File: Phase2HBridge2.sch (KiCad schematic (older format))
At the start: 42 parts, among them J1 CONN-01X06-TerminalBlock-3.5m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, J2 CONN-FASTON-0.250\"-1217861-1, J3 CONN-FASTON-0.250\"-1217861-1, J4 CONN-FASTON-0.250\"-1217861-1, J5 CONN-FASTON-0.250\"-1217861-1, Q1 FET-NCH-400V-26A-TO220-FDP26N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, Q2 FET-NCH-400V-26A-TO220-FDP26N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, Q3 FET-NCH-400V-26A-TO220-FDP26N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, Q4 FET-NCH-400V-26A-TO220-FDP26N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, U1 IC-Driver-HalfBridge-FAN7393A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

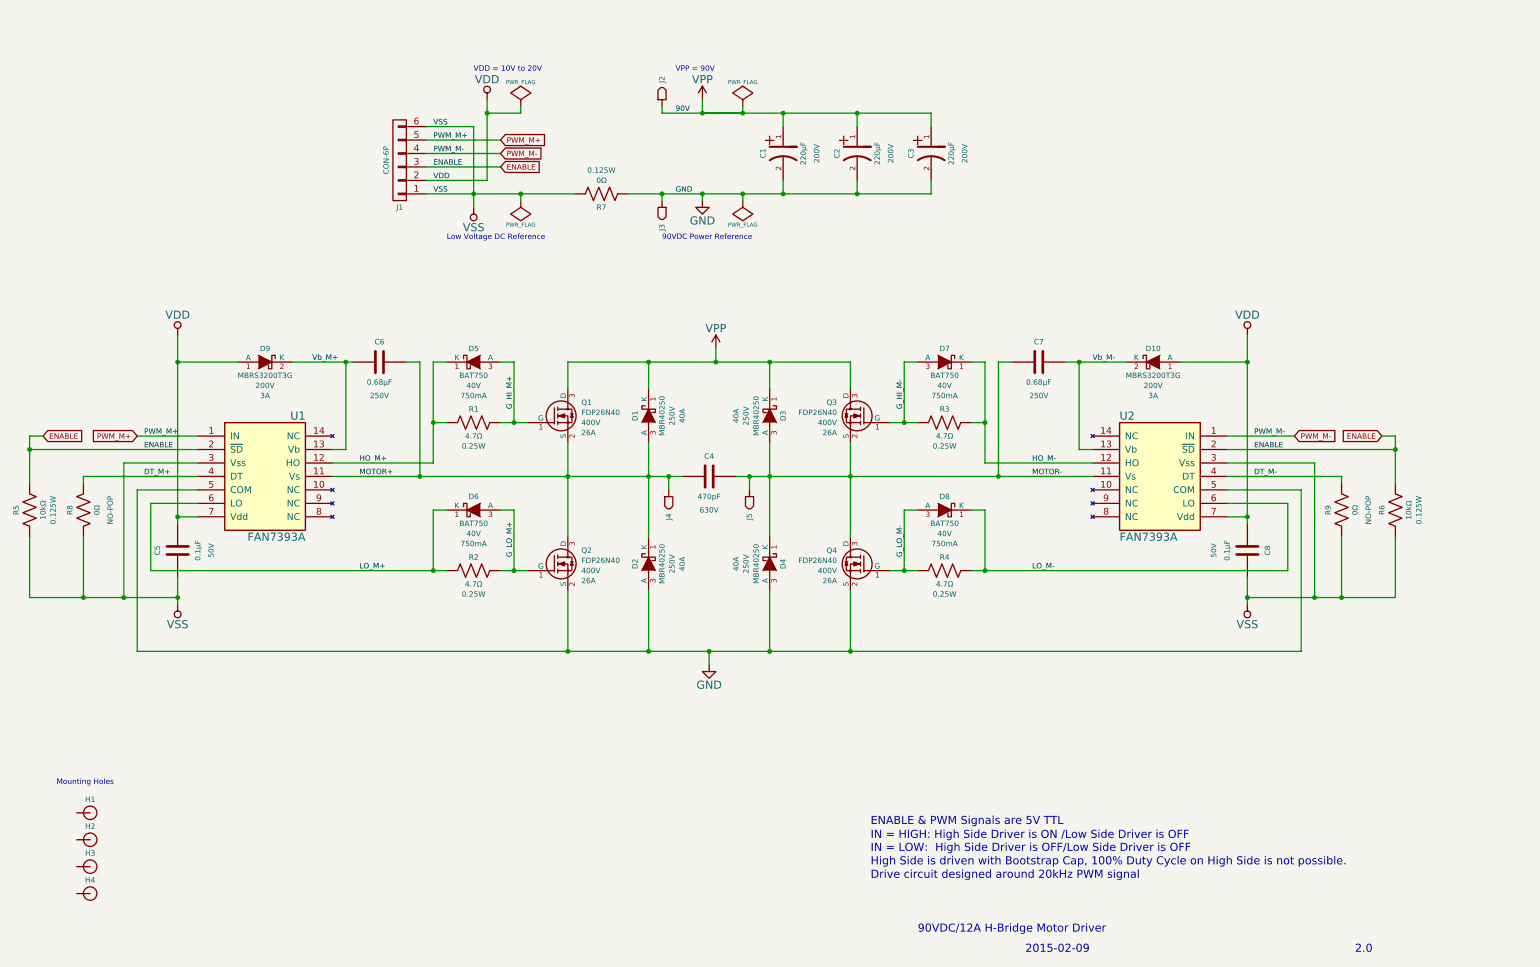
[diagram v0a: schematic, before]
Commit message: Finished Layout
Need to Verify Layout, add graphics, update refused locations, etc…
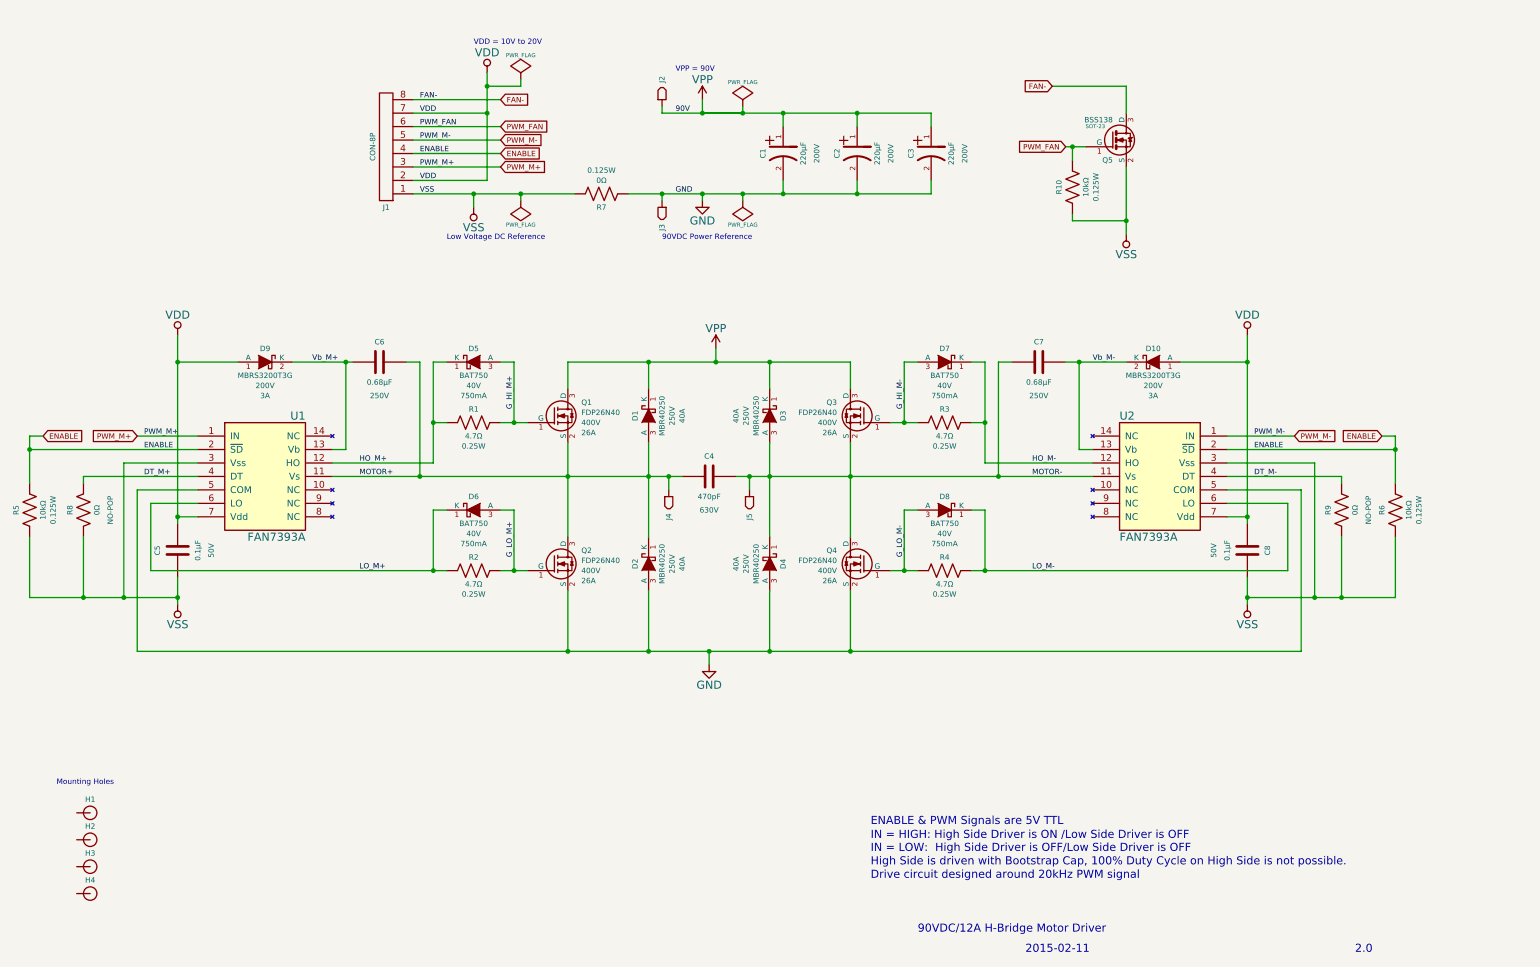
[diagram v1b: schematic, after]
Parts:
- removed J1: CONN-01X06-TerminalBlock-3.5mm-Side-1776275-6, Phase2HBridge2:CON-TerminalBlock-6Pos-Side-3.5MM-1776275-6, symbol CONN-01X06-TerminalBlock-3.5mm-Side-1776275-6
- added J1: CONN-01X08-TerminalBlock-3.5mm-Side-1776275-8, Phase2HBridge2:CON-TerminalBlock-8Pos-Side-3.5MM-1776275-8, symbol CONN-01X08-TerminalBlock-3.5mm-Side-1776275-8
- added Q5: BSS138, SOT-23, symbol BSS138
- added R10: RES-10k-.125W-1%-0805-ERJ-6ENF1002V, Resistors_SMD:R_0805, symbol RES-10k-.125W-1%-0805-ERJ-6ENF1002V
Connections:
- net ENABLE: now also J1.4 (P4)
- net PWM_M+: now also J1.3 (P3)
- net PWM_M-: now also J1.5 (P5)
- net VDD: now also J1.2 (P2), J1.7 (P7)
- net VSS: now also J1.1 (P1), Q5.2 (S), R10.2
- new net FAN-: J1.8 (P8), Q5.3 (D)
- new net PWM_FAN: J1.6 (P6), Q5.1 (G), R10.1
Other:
- note added: "2015-02-11"
- note removed: "2015-02-09"
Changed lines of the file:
@@
-$EndComp
-$Comp
-L CONN-01X06-TerminalBlock-3.5mm-Side-1776275-6 J1
-U 1 1 54D9000B
-P 3500 1750
-F 0 "J1" H 3500 2100 40  0000 C CNN
-F 1 "CONN-01X06-TerminalBlock-3.5mm-Side-1776275-6" H 3500 2300 40  0001 L CNN
-F 2 "Phase2HBridge2:CON-TerminalBlock-6Pos-Side-3.5MM-1776275-6" H 3500 1050 40  0001 L CNN
-F 3 "http://www.te.com/commerce/DocumentDelivery/DDEController?Action=srchrtrv&DocNm=1776275&DocType=Customer+Drawing&DocLang=English" H 3500 825 40  0001 L CNN
-F 4 "TE Connectivity" H 3500 950 40  0001 L CNN "MFG"
-F 5 "1776275-6" H 3500 900 40  0001 L CNN "MFGPN"
-F 6 "DigiKey" H 3500 700 40  0001 L CNN "CR1"
-F 7 "A98040-ND" H 3500 650 40  0001 L CNN "CR1PN"
-F 8 "-55°C:105°C" H 3500 525 40  0001 L CNN "Temp"
-F 9 "2015-02-09" H 3500 375 40  0001 L CNN "Created"
-F 10 "XXXX-XX-XX" H 3500 300 40  0001 L CNN "Verified"
-F 11 "CON-6P" V 3600 1750 40  0000 C CNN "Value.Display"
-	1    3500 1750
-	-1   0    0    1
 $EndComp
 $Comp
@@
 Connection ~ 5450 2000
 Wire Wire Line
-	3700 2000 4800 2000
+	3600 2000 4800 2000
 Wire Wire Line
 	5800 5400 5800 5500
@@
 	10200 4200 10200 5400
 Connection ~ 6850 5400
-Text Notes 4050 1100 0    40   ~ 0
+Text Notes 4050 900  0    40   ~ 0
 VDD = 10V to 20V
 Text Notes 5550 1100 0    40   ~ 0
@@
 Text Notes 950  6400 0    40   ~ 0
 Mounting Holes
-Text Label 3750 2000 0    40   ~ 0
+Text Label 3650 2000 0    40   ~ 0
 VSS
-Text Label 3750 1900 0    40   ~ 0
+Text Label 3650 1900 0    40   ~ 0
 VDD
 Text Label 5550 2000 0    40   ~ 0
@@
 Text Label 5550 1400 0    40   ~ 0
 90V
-Text Label 3750 1500 0    40   ~ 0
-VSS
+Text GLabel 4250 1800 2    40   Input ~ 0
+PWM_M+
 Text GLabel 4250 1600 2    40   Input ~ 0
+PWM_M-
+Text GLabel 4250 1700 2    40   Input ~ 0
+ENABLE
+Text Label 3650 1800 0    40   ~ 0
 PWM_M+
-Text GLabel 4250 1700 2    40   Input ~ 0
+Text Label 3650 1600 0    40   ~ 0
 PWM_M-
-Text GLabel 4250 1800 2    40   Input ~ 0
-ENABLE
-Wire Wire Line
-	3700 1600 4250 1600
-Wire Wire Line
-	3700 1700 4250 1700
-Wire Wire Line
-	3700 1800 4250 1800
-Text Label 3750 1600 0    40   ~ 0
-PWM_M+
-Text Label 3750 1700 0    40   ~ 0
-PWM_M-
-Text Label 3750 1800 0    40   ~ 0
+Text Label 3650 1700 0    40   ~ 0
 ENABLE
 Text GLabel 1550 3800 0    40   Input ~ 0
@@
 Text Label 1600 3800 0    40   ~ 0
 PWM_M+
-Wire Wire Line
-	4050 1500 4050 2100
 Connection ~ 4050 2000
-Wire Wire Line
-	3700 1500 4050 1500
 $Comp
 L VSS #PWR01
@@
 L VDD #PWR06
 U 1 1 54DAE29D
-P 4150 1300
-F 0 "#PWR06" H 4150 1150 60  0001 C CNN
-F 1 "VDD" H 4150 1450 60  0000 C CNN
-F 2 "" H 4150 1300 60  0000 C CNN
-F 3 "" H 4150 1300 60  0000 C CNN
-	1    4150 1300
+P 4150 1100
+F 0 "#PWR06" H 4150 950 60  0001 C CNN
+F 1 "VDD" H 4150 1250 60  0000 C CNN
+F 2 "" H 4150 1100 60  0000 C CNN
+F 3 "" H 4150 1100 60  0000 C CNN
+	1    4150 1100
 	1    0    0    -1
 $EndComp
@@
 $EndComp
 Wire Wire Line
-	4150 1300 4150 1900
-Wire Wire Line
-	4150 1900 3700 1900
+	4150 1100 4150 1900
+Wire Wire Line
+	4150 1900 3600 1900
 $Comp
 L VPP #PWR010
@@
 L PWR_FLAG #FLG013
 U 1 1 54DB25F7
-P 4400 1350
-F 0 "#FLG013" H 4400 1445 30  0001 C CNN
-F 1 "PWR_FLAG" H 4400 1530 30  0000 C CNN
-F 2 "" H 4400 1350 60  0000 C CNN
-F 3 "" H 4400 1350 60  0000 C CNN
-	1    4400 1350
+P 4400 1150
+F 0 "#FLG013" H 4400 1245 30  0001 C CNN
+F 1 "PWR_FLAG" H 4400 1330 30  0000 C CNN
+F 2 "" H 4400 1150 60  0000 C CNN
+F 3 "" H 4400 1150 60  0000 C CNN
+	1    4400 1150
 	1    0    0    -1
 $EndComp
@@
 Connection ~ 6050 2000
 Wire Wire Line
-	4400 1350 4400 1400
-Wire Wire Line
-	4400 1400 4150 1400
+	3600 1400 4150 1400
 Connection ~ 4150 1400
 Wire Wire Line
@@
 06 40 0A 85 A2 61 B1 58 ED 26 26 26 AD 3C 1E AF 59 20 10 D4 DA DB DB 57 D9 DA DA 3E B6 B6 B6 AE
 76 72 72 2A 73 70 70 78 2C 10 08 64 A6 A6 A6 8A 17 2B ED F3 C7 FF 03 F8 55 1F 08 EF 2D 21 89 00
-00 00 00 49 45 4E 44 AE 42 60 82 FF
+00 00 00 49 45 4E 44 AE 42 60 82 00
 EndData
 $EndBitmap
@@
 2.0\n
 Text Notes 8150 7650 0    60   ~ 0
-2015-02-09
+2015-02-11
 Text Notes 7000 6700 0    60   ~ 0
 ENABLE & PWM Signals are 5V TTL
@@
 Text Notes 7000 7100 0    60   ~ 0
 Drive circuit designed around 20kHz PWM signal
+$Comp
+L CONN-01X08-TerminalBlock-3.5mm-Side-1776275-8 J1
+U 1 1 54DC2CFE
+P 3400 1650
+F 0 "J1" H 3400 2100 40  0000 C CNN
+F 1 "CONN-01X08-TerminalBlock-3.5mm-Side-1776275-8" H 3400 2200 40  0001 L CNN
+F 2 "Phase2HBridge2:CON-TerminalBlock-8Pos-Side-3.5MM-1776275-8" H 3400 950 40  0001 L CNN
+F 3 "http://www.te.com/commerce/DocumentDelivery/DDEController?Action=srchrtrv&DocNm=1776275&DocType=Customer+Drawing&DocLang=English" H 3400 725 40  0001 L CNN
+F 4 "TE Connectivity" H 3400 850 40  0001 L CNN "MFG"
+F 5 "1776275-8" H 3400 800 40  0001 L CNN "MFGPN"
+F 6 "DigiKey" H 3400 600 40  0001 L CNN "CR1"
+F 7 "A98041-ND" H 3400 550 40  0001 L CNN "CR1PN"
+F 8 "-55°C:105°C" H 3400 425 40  0001 L CNN "Temp"
+F 9 "2015-02-11" H 3400 275 40  0001 L CNN "Created"
+F 10 "XXXX-XX-XX" H 3400 200 40  0001 L CNN "Verified"
+F 11 "CON-8P" V 3500 1650 40  0000 C CNN "Value.Display"
+F 12 "TERM BLOCK 8POS SIDE ENT 3.5MM" H 4300 2900 60  0001 C CNN "Description"
+	1    3400 1650
+	-1   0    0    1
+$EndComp
+Wire Wire Line
+	4050 2100 4050 2000
+Text GLabel 4250 1500 2    40   Input ~ 0
+PWM_FAN
+Wire Wire Line
+	3600 1500 4250 1500
+Text Label 3650 1500 0    40   ~ 0
+PWM_FAN
+Text Label 3650 1400 0    40   ~ 0
+VDD
+$Comp
+L BSS138 Q5
+U 1 1 54DC4EBA
+P 8800 1600
+F 0 "Q5" H 8800 1451 40  0000 R CNN
+F 1 "BSS138" H 8800 1750 40  0000 R CNN
+F 2 "SOT-23" H 8670 1702 29  0000 C CNN
+F 3 "" H 8800 1600 60  0000 C CNN
+	1    8800 1600
+	1    0    0    -1
+$EndComp
+Text GLabel 8450 1650 0    40   Input ~ 0
+PWM_FAN
+Wire Wire Line
+	8450 1650 8600 1650
+Text GLabel 4250 1300 2    40   Input ~ 0
+FAN-
+Wire Wire Line
+	4250 1300 3600 1300
+Text GLabel 8350 1200 0    40   Input ~ 0
+FAN-
+Wire Wire Line
+	8350 1200 8900 1200
+Wire Wire Line
+	8900 1200 8900 1400
+$Comp
+L VSS #PWR015
+U 1 1 54DC555A
+P 8900 2300
+F 0 "#PWR015" H 8900 2150 60  0001 C CNN
+F 1 "VSS" H 8900 2450 60  0000 C CNN
+F 2 "" H 8900 2300 60  0000 C CNN
+F 3 "" H 8900 2300 60  0000 C CNN
+	1    8900 2300
+	-1   0    0    1
+$EndComp
+Wire Wire Line
+	8900 1800 8900 2300
+$Comp
+L RES-10k-.125W-1%-0805-ERJ-6ENF1002V R10
+U 1 1 54DC569F
+P 8500 1950
+F 0 "R10" V 8400 1950 40  0000 C CNN
+F 1 "RES-10k-.125W-1%-0805-ERJ-6ENF1002V" H 8500 2300 40  0001 L CNN
+F 2 "Resistors_SMD:R_0805" H 8500 1500 40  0001 L CNN
+F 3 "http://industrial.panasonic.com/www-cgi/jvcr13pz.cgi?E+PZ+3+AOA0002+ERJ6ENF1002V+7+WW" H 8500 1250 40  0001 L CNN
+F 4 "10kΩ" V 8600 1950 40  0000 C CNN "Resistance"
+F 5 "Panasonic Electronic Components" H 8500 1350 40  0001 L CNN "MFG"
+F 6 "ERJ-6ENF1002V" H 8500 1300 40  0001 L CNN "MFGPN"
+F 7 "DigiKey" H 8500 1050 40  0001 L CNN "CR1"
+F 8 "P10.0KCCT-ND" H 8500 1000 40  0001 L CNN "CR1PN"
+F 9 "RES SMD 10K OHM 1% 1/8W 0805" H 8500 1550 40  0001 L CNN "Description"
+F 10 "-55°C:155°C" H 8500 950 40  0001 L CNN "Temp"
+F 11 "0.125W" V 8675 1950 40  0000 C CNN "Wattage"
+	1    8500 1950
+	1    0    0    -1
+$EndComp
+Wire Wire Line
+	8500 2150 8500 2200
+Wire Wire Line
+	8500 2200 8900 2200
+Connection ~ 8900 2200
+Wire Wire Line
+	8500 1750 8500 1650
+Connection ~ 8500 1650
+Text Label 3650 1300 0    40   ~ 0
+FAN-
+Wire Wire Line
+	4400 1150 4400 1200
+Wire Wire Line
+	4400 1200 4150 1200
+Connection ~ 4150 1200
+Wire Wire Line
+	4250 1600 3600 1600
+Wire Wire Line
+	3600 1800 4250 1800
+Wire Wire Line
+	3600 1700 4250 1700
 $EndSCHEMATC

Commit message: Finished Design
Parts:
- added D11: DIODE-SCH-40V-750mA-BAT750, Transistors_SMD:sot23, symbol DIODE-SCH-40V-750mA-BAT750
- Q1, Q2, Q3, Q4: CR1PN FAN7393AMXCT-ND -> FDP26N40-ND; MFGPN FAN7393AMX -> FDP26N40
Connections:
- net FAN-: now also D11.3 (A)
- net VDD: now also D11.1 (K)
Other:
- moved on the sheet: Q5, R10
